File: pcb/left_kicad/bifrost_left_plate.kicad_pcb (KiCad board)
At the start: 2 copper layers, 148.8 x 87.6 mm, 22 parts

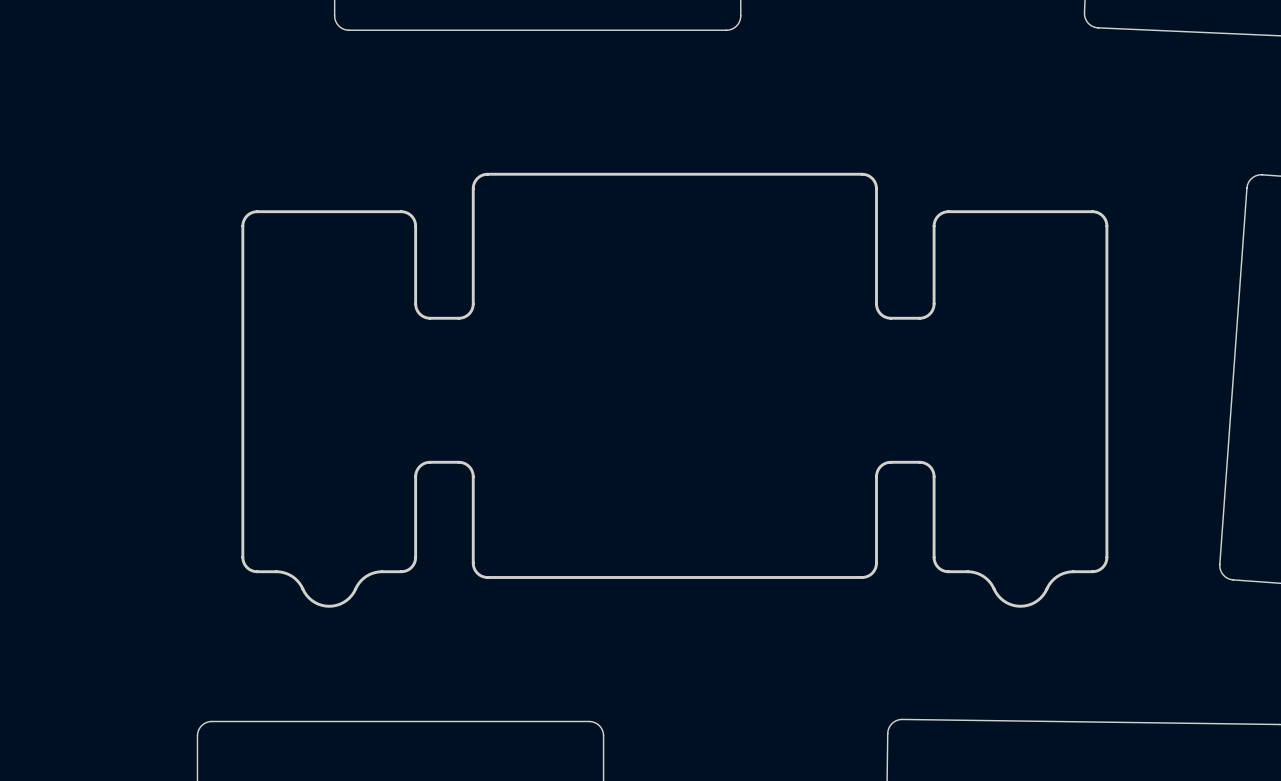
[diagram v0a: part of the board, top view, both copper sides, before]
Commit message: Update KiCad keyboard designs
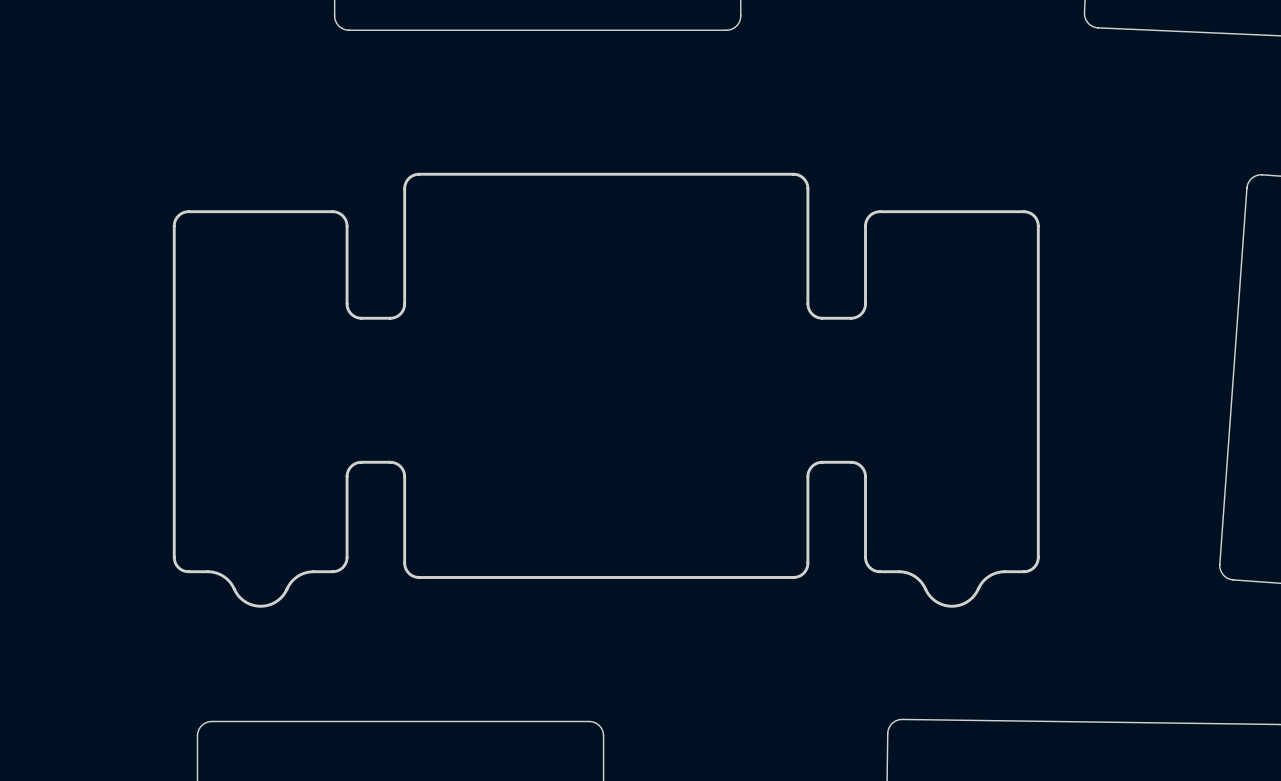
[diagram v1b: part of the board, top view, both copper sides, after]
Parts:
- PH50: footprint Smidr:Plate_Smidr_Stab_Hole_Gateron_LP_2.25u -> Smidr:Plate_Smidr_Stab_Hole_Gateron_LP_2u
- moved PH50 2.38 mm to (9.53, 38.1)
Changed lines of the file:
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@@
 		(embedded_fonts no)
 	)
-	(footprint "Smidr:Plate_Smidr_Stab_Hole_Gateron_LP_2.25u"
+	(footprint "Smidr:Plate_Smidr_Stab_Hole_Gateron_LP_2u"
 		(layer "F.Cu")
-		(at 11.90625 38.1 180)
+		(at 9.525 38.1 180)
 		(property "Reference" "PH50"
-			(at 7 8.099999 0)
+			(at 7 8.1 180)
 			(layer "F.SilkS")
 			(hide yes)
@@
 		)
 		(property "Value" "R2C6"
-			(at -7.4 -8.1 0)
+			(at -7.4 -8.1 180)
 			(layer "F.Fab")
 			(hide yes)
@@
 		)
 		(fp_line
-			(start 9.5 -6.800001)
-			(end 10.16697 -6.800001)
+			(start 9.5 -6.8)
+			(end 10.16697 -6.8)
 			(stroke
 				(width 0.1)
@@
 		(fp_line
 			(start 8.5 2)
-			(end 7.499999 2)
+			(end 7.5 2)
 			(stroke
 				(width 0.1)
@@
 		)
 		(fp_line
-			(start 7 2.499999)
-			(end 7 6.500001)
-			(stroke
-				(width 0.1)
-				(type default)
-			)
-			(layer "Edge.Cuts")
-		)
-		(fp_line
-			(start 7 -6.500001)
+			(start 7 2.5)
+			(end 7 6.5)
+			(stroke
+				(width 0.1)
+				(type default)
+			)
+			(layer "Edge.Cuts")
+		)
+		(fp_line
+			(start 7 -6.5)
 			(end 7 -3.5)
 			(stroke
@@
 		)
 		(fp_line
-			(start 6.500001 7)
-			(end -6.500001 7)
-			(stroke
-				(width 0.1)
-				(type default)
-			)
-			(layer "Edge.Cuts")
-		)
-		(fp_line
-			(start -6.500001 -7)
-			(end 6.500001 -7)
-			(stroke
-				(width 0.1)
-				(type default)
-			)
-			(layer "Edge.Cuts")
-		)
-		(fp_line
-			(start -7 6.500001)
-			(end -7 2.499999)
+			(start 6.5 7)
+			(end -6.5 7)
+			(stroke
+				(width 0.1)
+				(type default)
+			)
+			(layer "Edge.Cuts")
+		)
+		(fp_line
+			(start -6.5 -7)
+			(end 6.5 -7)
+			(stroke
+				(width 0.1)
+				(type default)
+			)
+			(layer "Edge.Cuts")
+		)
+		(fp_line
+			(start -7 6.5)
+			(end -7 2.5)
 			(stroke
 				(width 0.1)
@@
 		(fp_line
 			(start -7 -3.5)
-			(end -7 -6.500001)
-			(stroke
-				(width 0.1)
-				(type default)
-			)
-			(layer "Edge.Cuts")
-		)
-		(fp_line
-			(start -7.499999 2)
+			(end -7 -6.5)
+			(stroke
+				(width 0.1)
+				(type default)
+			)
+			(layer "Edge.Cuts")
+		)
+		(fp_line
+			(start -7.5 2)
 			(end -8.5 2)
 			(stroke
@@
 		)
 		(fp_line
-			(start -10.16697 -6.800001)
-			(end -9.5 -6.800001)
+			(start -10.16697 -6.8)
+			(end -9.5 -6.8)
 			(stroke
 				(width 0.1)
@@
 		(fp_arc
 			(start 14.5 -6.8)
-			(mid 14.853553 -6.653552)
+			(mid 14.853553 -6.653553)
 			(end 15 -6.3)
 			(stroke
@@
 		(fp_arc
 			(start 13.83303 -6.8)
-			(mid 13.285307 -6.96334)
+			(mid 13.285308 -6.96334)
 			(end 12.916515 -7.4)
 			(stroke
@@
 		(fp_arc
 			(start 11.083485 -7.4)
-			(mid 10.714691 -6.96334)
-			(end 10.16697 -6.800001)
+			(mid 10.714692 -6.96334)
+			(end 10.16697 -6.8)
 			(stroke
 				(width 0.1)
@@
 		(fp_arc
 			(start 9 -3.5)
-			(mid 8.853552 -3.146447)
+			(mid 8.853553 -3.146447)
 			(end 8.5 -3)
 			(stroke
@@
 			(start 9 -6.3)
 			(mid 9.146447 -6.653553)
-			(end 9.5 -6.800001)
+			(end 9.5 -6.8)
 			(stroke
 				(width 0.1)
@@
 		)
 		(fp_arc
-			(start 7 6.500001)
+			(start 7 6.5)
 			(mid 6.853553 6.853553)
-			(end 6.500001 7)
-			(stroke
-				(width 0.1)
-				(type default)
-			)
-			(layer "Edge.Cuts")
-		)
-		(fp_arc
-			(start 7 2.499999)
+			(end 6.5 7)
+			(stroke
+				(width 0.1)
+				(type default)
+			)
+			(layer "Edge.Cuts")
+		)
+		(fp_arc
+			(start 7 2.5)
 			(mid 7.146447 2.146447)
-			(end 7.499999 2)
-			(stroke
-				(width 0.1)
-				(type default)
-			)
-			(layer "Edge.Cuts")
-		)
-		(fp_arc
-			(start 6.500001 -7)
+			(end 7.5 2)
+			(stroke
+				(width 0.1)
+				(type default)
+			)
+			(layer "Edge.Cuts")
+		)
+		(fp_arc
+			(start 6.5 -7)
 			(mid 6.853553 -6.853553)
-			(end 7 -6.500001)
-			(stroke
-				(width 0.1)
-				(type default)
-			)
-			(layer "Edge.Cuts")
-		)
-		(fp_arc
-			(start -6.500001 7)
+			(end 7 -6.5)
+			(stroke
+				(width 0.1)
+				(type default)
+			)
+			(layer "Edge.Cuts")
+		)
+		(fp_arc
+			(start -6.5 7)
 			(mid -6.853553 6.853553)
-			(end -7 6.500001)
+			(end -7 6.5)
 			(stroke
 				(width 0.1)
@@
 		)
 		(fp_arc
-			(start -7 -6.500001)
+			(start -7 -6.5)
 			(mid -6.853553 -6.853553)
-			(end -6.500001 -7)
-			(stroke
-				(width 0.1)
-				(type default)
-			)
-			(layer "Edge.Cuts")
-		)
-		(fp_arc
-			(start -7.499999 2)
+			(end -6.5 -7)
+			(stroke
+				(width 0.1)
+				(type default)
+			)
+			(layer "Edge.Cuts")
+		)
+		(fp_arc
+			(start -7.5 2)
 			(mid -7.146447 2.146447)
-			(end -7 2.499999)
+			(end -7 2.5)
 			(stroke
 				(width 0.1)
@@
 		(fp_arc
 			(start -8.5 -3)
-			(mid -8.853552 -3.146447)
+			(mid -8.853553 -3.146447)
 			(end -9 -3.5)
 			(stroke
@@
 		)
 		(fp_arc
-			(start -9.5 -6.800001)
+			(start -9.5 -6.8)
 			(mid -9.146447 -6.653553)
 			(end -9 -6.3)
@@
 		)
 		(fp_arc
-			(start -10.16697 -6.800001)
+			(start -10.16697 -6.8)
 			(mid -10.714705 -6.963328)
 			(end -11.083485 -7.4)
@@
 		(fp_arc
 			(start -15 -6.3)
-			(mid -14.853553 -6.653552)
+			(mid -14.853553 -6.653553)
 			(end -14.5 -6.8)
 			(stroke
@@
 		)
 		(fp_line
-			(start 21.43125 9.525)
-			(end 21.43125 -9.525)
+			(start 19.05 9.525)
+			(end 19.05 -9.525)
 			(stroke
 				(width 0.15)
@@
 		)
 		(fp_line
-			(start 21.43125 -9.525)
-			(end -21.43125 -9.525)
+			(start 19.05 -9.525)
+			(end -19.05 -9.525)
 			(stroke
 				(width 0.15)
@@
 		)
 		(fp_line
-			(start -21.43125 9.525)
-			(end 21.43125 9.525)
+			(start -19.05 9.525)
+			(end 19.05 9.525)
 			(stroke
 				(width 0.15)
@@
 		)
 		(fp_line
-			(start -21.43125 -9.525)
-			(end -21.43125 9.525)
+			(start -19.05 -9.525)
+			(end -19.05 9.525)
 			(stroke
 				(width 0.15)

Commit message: Update PCB designs
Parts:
- added ?: , , F.Cu at (-12.7, -6.35)
- added ?: , , F.Cu at (-15.9, 44.5)
- added ?: , , F.Cu at (-19.1, 0.00)
- added ?: , , F.Cu at (-12.7, 12.7)
- added ?: , , F.Cu at (-15.9, 0.00)
- added ?: , , F.Cu at (-15.9, 3.17)
- added ?: , , F.Cu at (-12.7, 28.6)
- added ?: , , F.Cu at (-12.7, 25.4)
- added ?: , , F.Cu at (-19.1, 22.2)
- added ?: , , F.Cu at (-19.1, 54.0)
- added ?: , , F.Cu at (-19.1, -3.17)
- added ?: , , F.Cu at (-15.9, 41.3)
- added ?: , , F.Cu at (-12.7, 9.53)
- added ?: , , F.Cu at (-12.7, 60.3)
- added ?: , , F.Cu at (-12.7, 34.9)
- added ?: , , F.Cu at (-12.7, 15.9)
- added ?: , , F.Cu at (-12.7, 3.17)
- added ?: , , F.Cu at (-15.9, 63.5)
- added ?: , , F.Cu at (-12.7, 44.5)
- added ?: , , F.Cu at (-15.9, 38.1)
- added ?: , , F.Cu at (-15.9, 15.9)
- added ?: , , F.Cu at (-12.7, 31.8)
- added ?: , , F.Cu at (-15.9, 28.6)
- added ?: , , F.Cu at (-15.9, 60.3)
- added ?: , , F.Cu at (-19.1, 50.8)
- added ?: , , F.Cu at (-15.9, 25.4)
- added ?: , , F.Cu at (-12.7, -3.17)
- added ?: , , F.Cu at (-12.7, 22.2)
- added ?: , , F.Cu at (-12.7, 63.5)
- added ?: , , F.Cu at (-15.9, 31.8)
- added ?: , , F.Cu at (-19.1, 15.9)
- added ?: , , F.Cu at (-12.7, 0.00)
- added ?: , , F.Cu at (-19.1, 19.1)
- added ?: , , F.Cu at (-15.9, 54.0)
- added ?: , , F.Cu at (-19.1, 38.1)
- added ?: , , F.Cu at (-12.7, 47.6)
- added ?: , , F.Cu at (-15.9, 6.35)
- added ?: , , F.Cu at (-15.9, 34.9)
- added ?: , , F.Cu at (-19.1, 25.4)
- added ?: , , F.Cu at (-19.1, 12.7)
- added ?: , , F.Cu at (-19.1, 9.53)
- added ?: , , F.Cu at (-12.7, 19.1)
- added ?: , , F.Cu at (-15.9, 12.7)
- added ?: , , F.Cu at (-15.9, -6.35)
- added ?: , , F.Cu at (-19.1, 44.5)
- added ?: , , F.Cu at (-19.1, 41.3)
- added ?: , , F.Cu at (-19.1, 28.6)
- added ?: , , F.Cu at (-15.9, 22.2)
- added ?: , , F.Cu at (-15.9, 9.53)
- added ?: , , F.Cu at (-19.1, 6.35)
- added ?: , , F.Cu at (-15.9, 50.8)
- added ?: , , F.Cu at (-12.7, 41.3)
- added ?: , , F.Cu at (-12.7, 6.35)
- added ?: , , F.Cu at (-15.9, 47.6)
- added ?: , , F.Cu at (-19.1, 3.17)
- added ?: , , F.Cu at (-15.9, 19.1)
- added ?: , , F.Cu at (-12.7, 57.1)
- added ?: , , F.Cu at (-19.1, 31.8)
- added ?: , , F.Cu at (-12.7, 54.0)
- added ?: , , F.Cu at (-15.9, 57.1)
- added ?: , , F.Cu at (-19.1, 34.9)
- added ?: , , F.Cu at (-12.7, 50.8)
- added ?: , , F.Cu at (-19.1, 47.6)
- added ?: , , F.Cu at (-19.1, 57.1)
- added ?: , , F.Cu at (-12.7, 38.1)
- added ?: , , F.Cu at (-19.1, 60.3)

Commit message: Update PCB and case designs
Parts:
- added REF**: MountingHole_2.2mm_M2, MountingHole:MountingHole_2.2mm_M2, F.Cu at (192.1, 61.2)
- added REF**: MountingHole_2.2mm_M2, MountingHole:MountingHole_2.2mm_M2, F.Cu at (218.3, 130.9)
- added REF**: MountingHole_2.2mm_M2, MountingHole:MountingHole_2.2mm_M2, F.Cu at (75.4, 50.0)
- added REF**: MountingHole_2.2mm_M2, MountingHole:MountingHole_2.2mm_M2, F.Cu at (75.4, 126.2)
- PH1: value R1C0 -> 1.5U
- PH10: value R4C6 -> 1.25U
- PH11: value R1C1 -> 1U
- PH12: value R1C2 -> 1U
- PH13: value R1C3 -> 1U
- PH14: value R1C4 -> 1U
- PH15: value R1C5 -> 1U
- PH21: value R2C1 -> 1U
- PH22: value R2C2 -> 1U
- PH23: value R2C3 -> 1U
- PH24: value R2C4 -> 1U
- PH25: value R2C5 -> 1U
- PH31: value R3C1 -> 1U
- PH32: value R3C2 -> 1U
- PH33: value R3C3 -> 1U
- PH34: value R3C4 -> 1U
- PH35: value R3C5 -> 1U
- PH47: value R4C0 -> 1.25U
- PH48: value R4C1 -> 1.25U
- PH50: value R2C6 -> 2U
- PH7: value R2C0 -> 1.75U
- moved ? 111.7 mm to (81.8, 53.2)
- moved ? 111.7 mm to (81.8, 72.2)
- moved ? 111.7 mm to (81.8, 88.1)
- moved ? 111.7 mm to (81.8, 84.9)
- moved ? 111.7 mm to (81.8, 69.1)
- moved ? 111.7 mm to (81.8, 119.9)
- moved ? 111.7 mm to (81.8, 94.5)
- moved ? 111.7 mm to (81.8, 75.4)
- moved ? 111.7 mm to (81.8, 62.7)
- moved ? 111.7 mm to (81.8, 104.0)
- moved ? 111.7 mm to (81.8, 91.3)
- moved ? 111.7 mm to (81.8, 56.4)
- moved ? 111.7 mm to (81.8, 81.8)
- moved ? 111.7 mm to (81.8, 123.0)
- moved ? 111.7 mm to (81.8, 59.5)
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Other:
- outline, holes or cut-outs redrawn

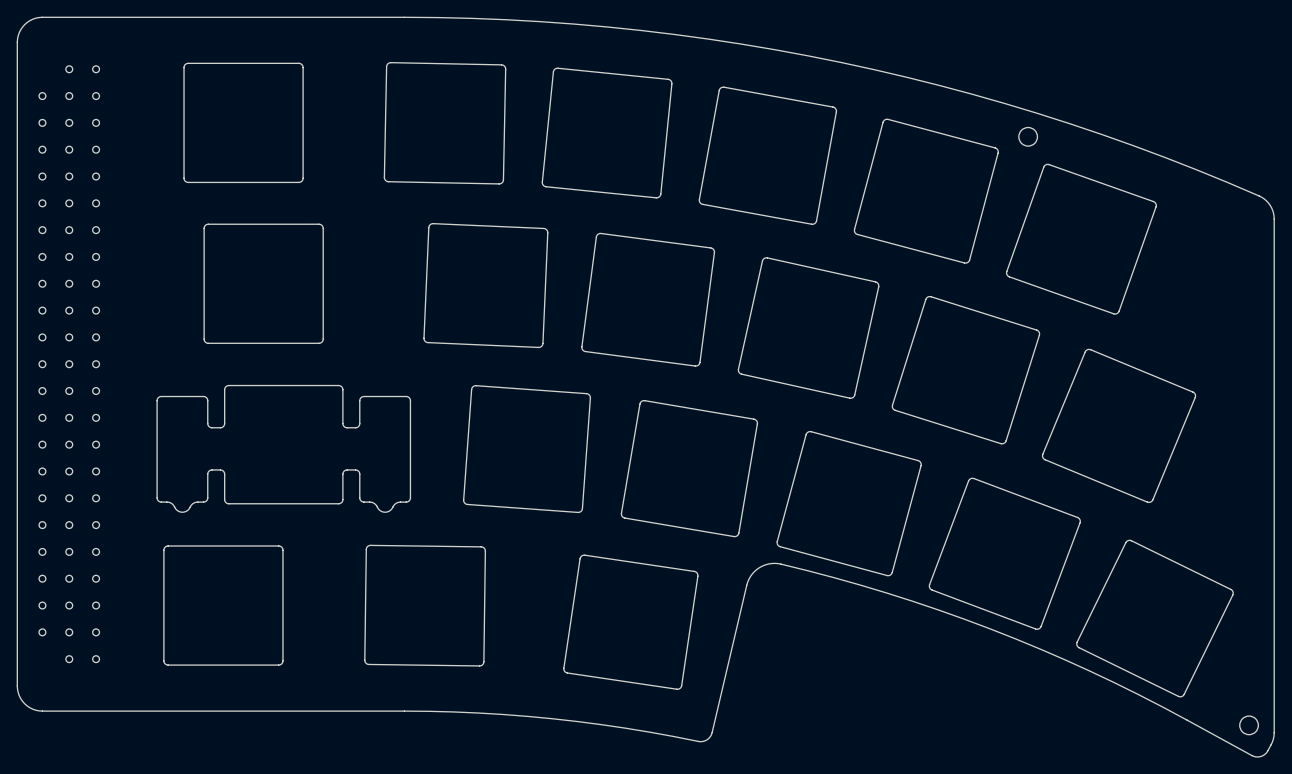
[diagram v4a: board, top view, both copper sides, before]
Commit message: Update case and plate designs
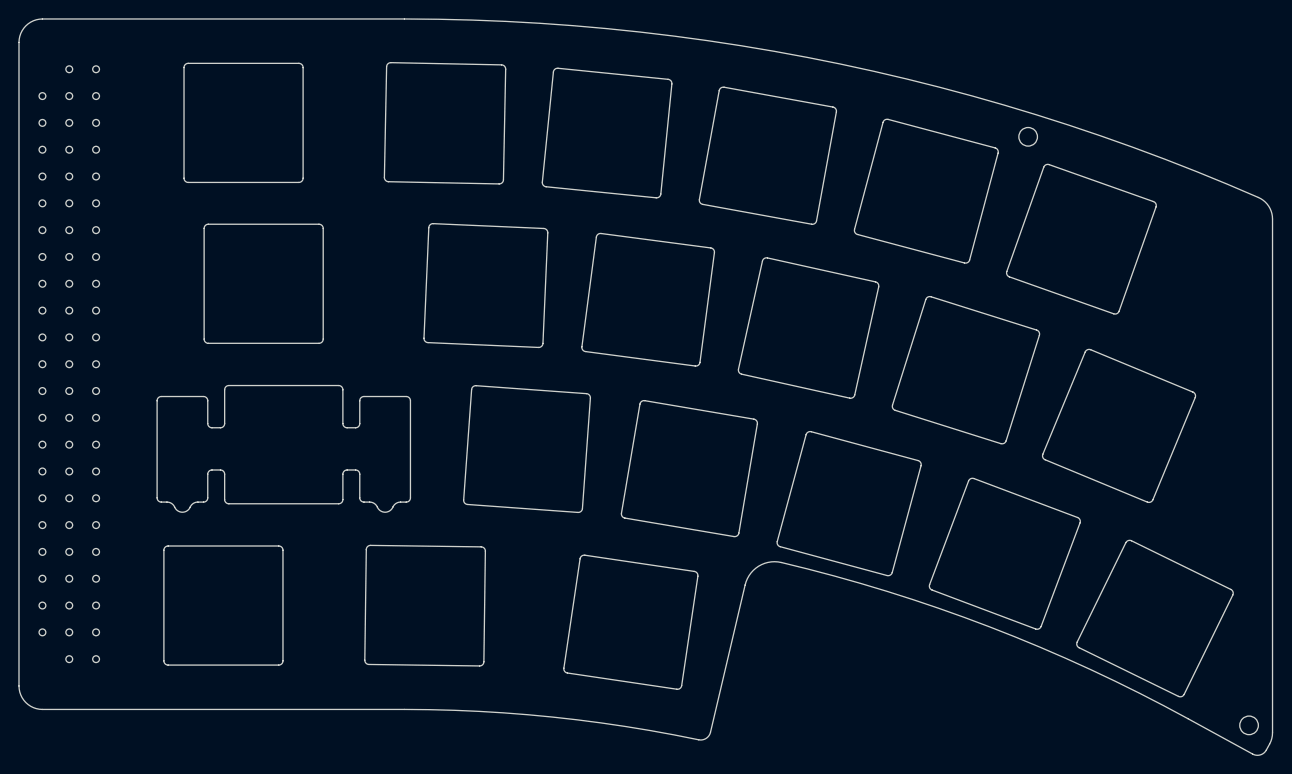
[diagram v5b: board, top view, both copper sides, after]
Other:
- board size 148.8 x 87.6 mm -> 148.4 x 87.2 mm
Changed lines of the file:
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@@
 	)
 	(gr_line
-		(start 72.429188 50.006249)
-		(end 72.429188 126.20625)
+		(start 72.628124 50.00625)
+		(end 72.628124 126.20625)
 		(stroke
 			(width 0.1)
@@
 	)
 	(gr_arc
-		(start 72.429188 50.006249)
-		(mid 73.301003 47.901501)
-		(end 75.40575 47.029686)
+		(start 72.628124 50.00625)
+		(mid 73.441818 48.041819)
+		(end 75.406249 47.228125)
 		(stroke
 			(width 0.1)
@@
 	)
 	(gr_arc
-		(start 75.40575 129.182811)
-		(mid 73.301033 128.31098)
-		(end 72.429188 126.20625)
+		(start 75.406249 128.984375)
+		(mid 73.441833 128.170666)
+		(end 72.628124 126.20625)
 		(stroke
 			(width 0.1)
@@
 	)
 	(gr_line
-		(start 75.40575 129.182811)
-		(end 118.26825 129.182812)
+		(start 75.406249 128.984375)
+		(end 118.26875 128.984375)
 		(stroke
 			(width 0.1)
@@
 	)
 	(gr_line
-		(start 118.26825 47.029688)
-		(end 75.40575 47.029686)
+		(start 118.26875 47.228125)
+		(end 75.406249 47.228125)
 		(stroke
 			(width 0.1)
@@
 	)
 	(gr_arc
-		(start 118.26825 47.029688)
-		(mid 169.964299 52.374889)
-		(end 219.473027 68.184335)
+		(start 118.26875 47.228125)
+		(mid 169.924198 52.569129)
+		(end 219.394042 68.366159)
 		(stroke
 			(width 0.1)
@@
 	)
 	(gr_arc
-		(start 118.26825 129.182812)
-		(mid 135.76008 130.082398)
-		(end 153.06734 132.77166)
+		(start 118.26875 128.984375)
+		(mid 135.780936 129.885011)
+		(end 153.108339 132.5774)
 		(stroke
 			(width 0.1)
@@
 	)
 	(gr_arc
-		(start 154.703021 131.729773)
-		(mid 154.097101 132.583437)
-		(end 153.06734 132.77166)
+		(start 154.510352 131.684353)
+		(mid 153.990999 132.416048)
+		(end 153.108339 132.5774)
 		(stroke
 			(width 0.1)
@@
 	)
 	(gr_line
-		(start 154.703021 131.729773)
-		(end 158.803389 114.29094)
+		(start 154.510352 131.684353)
+		(end 158.61072 114.24552)
 		(stroke
 			(width 0.1)
@@
 	)
 	(gr_arc
-		(start 158.803389 114.29094)
-		(mid 160.314197 112.193175)
-		(end 162.866274 111.780814)
+		(start 158.61072 114.24552)
+		(mid 160.210405 112.024365)
+		(end 162.912598 111.587739)
 		(stroke
 			(width 0.1)
@@
 	)
 	(gr_arc
-		(start 162.866274 111.780814)
-		(mid 187.527647 119.406894)
-		(end 210.951721 130.253698)
+		(start 162.912598 111.587739)
+		(mid 187.599308 119.22166)
+		(end 211.047452 130.079605)
 		(stroke
 			(width 0.1)
@@
 	)
 	(gr_line
-		(start 210.951721 130.253698)
-		(end 218.611841 134.44384)
+		(start 211.047452 130.079605)
+		(end 218.707571 134.269746)
 		(stroke
 			(width 0.1)
@@
 	)
 	(gr_arc
-		(start 219.473027 68.184335)
-		(mid 220.771614 69.282102)
-		(end 221.257313 70.911678)
+		(start 219.394042 68.366159)
+		(mid 220.606086 69.390731)
+		(end 221.059374 70.911679)
 		(stroke
 			(width 0.1)
@@
 	)
 	(gr_arc
-		(start 220.49711 133.891798)
-		(mid 219.668808 134.558272)
-		(end 218.611841 134.44384)
+		(start 220.323517 133.796567)
+		(mid 219.613548 134.367808)
+		(end 218.707571 134.269746)
 		(stroke
 			(width 0.1)
@@
 	)
 	(gr_line
-		(start 220.49711 133.891798)
-		(end 220.892155 133.169605)
+		(start 220.323517 133.796567)
+		(end 220.71856 133.074375)
 		(stroke
 			(width 0.1)
@@
 	)
 	(gr_arc
-		(start 221.257312 131.741148)
-		(mid 221.164577 132.478343)
-		(end 220.892155 133.169605)
+		(start 221.059374 131.741147)
+		(mid 220.972833 132.429201)
+		(end 220.71856 133.074375)
 		(stroke
 			(width 0.1)
@@
 	)
 	(gr_line
-		(start 221.257312 131.741148)
-		(end 221.257313 70.911678)
+		(start 221.059374 131.741147)
+		(end 221.059374 70.911679)
 		(stroke
 			(width 0.1)
@@
 	)
 	(group ""
-		(members "035129f6-44f5-4098-8585-2bb5eca8053b" "04bad7a8-d23b-473a-87e6-3ea9995b09fa"
-			"2c9cdff6-737b-4e4e-8540-dd30cda8b9f7" "3a8b303f-9ac4-427d-87fd-341758055fe8"
-			"3e2e4664-785c-4709-83a6-972aaf3d87d3" "3f1b03dd-3294-44f6-b604-8d031351d43c"
-			"4a410c5e-049e-4d26-8ae1-f35a946b35d0" "52252277-7124-4669-8c4c-382d3ee4088d"
-			"5780ac79-e8f9-4bae-889a-f1bfce610d04" "61cc0f87-8aad-41d3-8b32-8e1101968101"
-			"6f6d0b95-5a58-44bd-b643-5f992a841002" "789e54af-41cd-4df6-aa12-6d046a22b771"
-			"7c9c5ac0-a006-4b18-8219-a1370a58e293" "ba43e523-64f8-4f6c-8ddc-288e0f14003a"
-			"cc1d0635-90bb-40f7-bc17-1b3c13e5b50b" "ceb0cfd2-e2cd-4822-9e27-51623d61c0cc"
-			"de4601b7-ff02-4d66-b169-3668dd3f28cc"
+		(members "020d2139-f3e4-412b-9f7d-e20a91c65915" "074d74d9-8e82-461e-98ea-6acc7faba942"
+			"19cbae4e-56ff-4e48-8aa7-7e0389cace1b" "28dd6a4b-737f-453f-9782-73c85eea0b5b"
+			"313ea742-35f1-4d5b-a6f0-daa44dd47a15" "31efc937-3858-4bd7-97a4-ab23e8e250d9"
+			"55c00b13-81b6-48fe-821e-42da8a9f16cc" "59be90ce-8a4d-44df-8656-00ac865135f5"
+			"6c852f36-d9d7-4b9a-b5d6-7d8fab5f3cad" "6fb6ef81-db41-4feb-94bc-4e21cfd338df"
+			"74cda921-9dd5-4b2f-b8cc-a65d48416ef4" "816d6980-befd-4bb2-a61c-30580ea67fd1"
+			"81a88573-3525-403b-a232-780dba4df5b2" "a076d07a-2396-4de9-b88d-b6e784f33dda"
+			"e7e21749-b5c8-4b51-82a7-9ecfe5321f93" "ee82b7d8-f6d2-4e5b-b6cc-bda832b1c4b9"
+			"fb39a80c-0a19-489a-8e12-9eaf08926d97"
 		)
 	)
